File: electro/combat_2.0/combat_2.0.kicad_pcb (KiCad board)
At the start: 2 copper layers, 110.5 x 45.7 mm, 51 parts, among them J1 BATT, J12 MOT_WPN, J13 Conn_02x09_Odd_Even, J14 Conn_02x09_Odd_Even, J2 Conn_01x02_Socket, J3 UART, J4 Conn_01x03_Pin, J5 Conn_01x03_Pin, J6 Conn_01x03_Socket, J7 Conn_01x03_Socket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

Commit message: small improvements
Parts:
- R6: moved to F.Cu
- moved J6 1.91 mm to (59.1, 107.9)
- moved REF** 0.64 mm to (112.4, 123.2)
- moved REF** 0.64 mm to (112.4, 83.8)
- moved Q2 0.11 mm to (152.3, 111.7)
- moved C18 0.11 mm to (157.1, 91.7)
- moved D3 0.11 mm to (151.0, 89.7)
- moved Q1 0.11 mm to (159.2, 111.8)
- moved Q3 0.11 mm to (154.8, 104.2)
- moved Q4 0.11 mm to (154.9, 98.2)
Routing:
- net /weapon_motor/MOTOR_PWR: track 29.4 -> 28.2 mm
- net /PWM_WEAPON: track 78.9 -> 78.1 mm
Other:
- board size 110.5 x 45.7 mm -> 109.1 x 45.7 mm

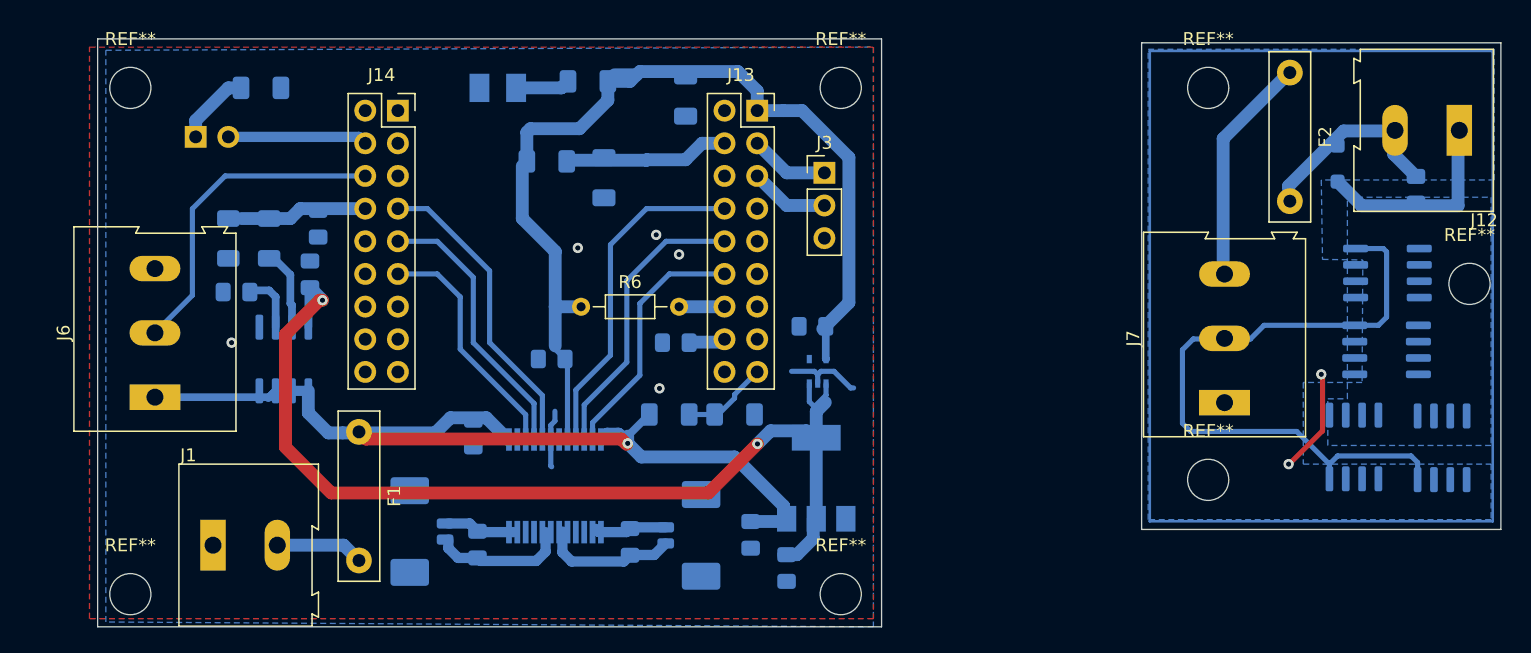
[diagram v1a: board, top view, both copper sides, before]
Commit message: Change in mosfets routing
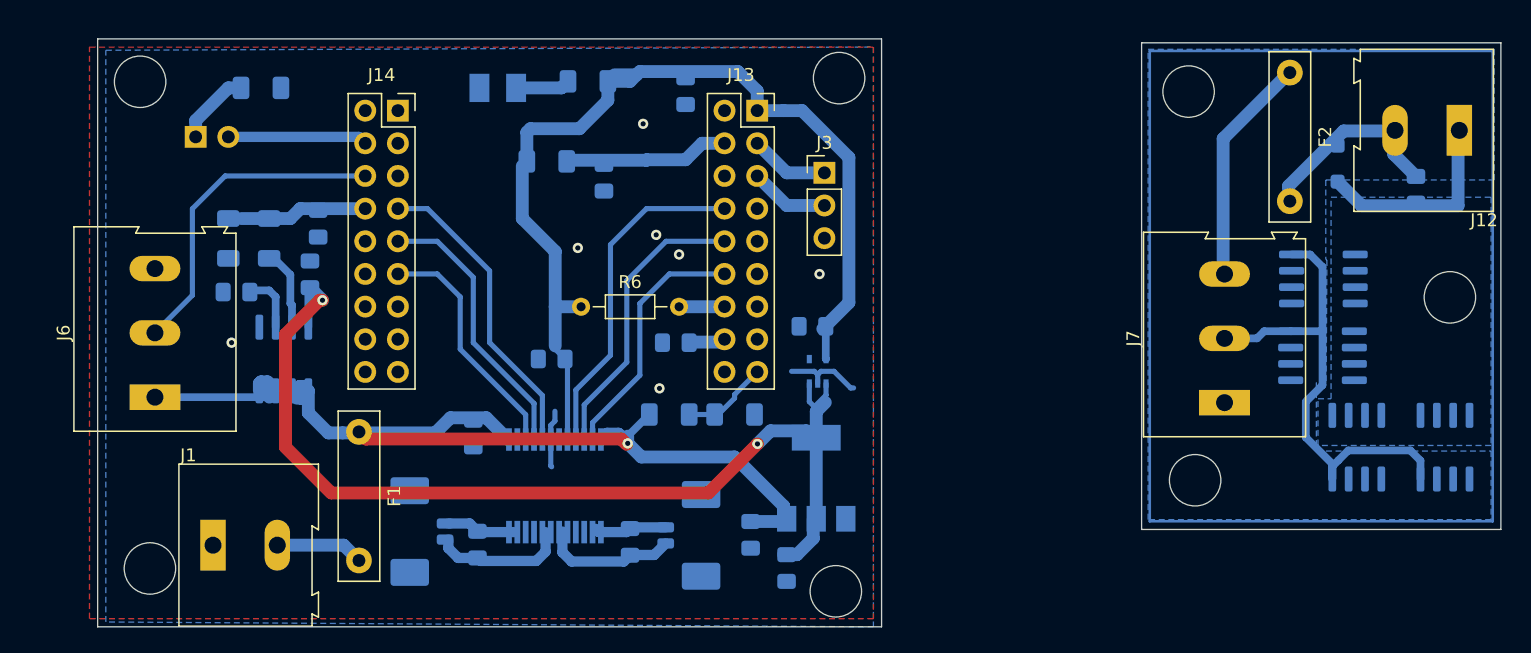
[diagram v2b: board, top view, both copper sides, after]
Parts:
- removed REF** (x7): MountingHole_3.2mm_M3_DIN965, MountingHole:MountingHole_3.2mm_M3_DIN965
- C1, C3: footprint Capacitor_SMD:C_1206_3216Metric_Pad1.33x1.80mm_HandSolder -> Capacitor_SMD:C_0805_2012Metric_Pad1.18x1.45mm_HandSolder
- moved Q3 5.00 mm to (149.9, 104.6)
- moved Q4 5.00 mm to (149.9, 98.7)
- moved C3 0.38 mm to (100.3, 84.1)
- moved Q1 0.23 mm to (159.4, 111.8)
- moved Q2 0.23 mm to (152.5, 111.8)
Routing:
- net /PWM_WEAPON: track 78.1 -> 64.0 mm
- net GND: track 18.8 -> 10.7 mm
- net /weapon_motor/MOTOR_PWR: track 28.2 -> 30.8 mm
- net +8V: track 65.2 -> 66.7 mm
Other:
- outline, holes or cut-outs redrawn
